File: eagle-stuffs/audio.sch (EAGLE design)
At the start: 35 parts, among them IC1 SSM2211SZ, IC2 TL084P, IC4 DS1804-10k

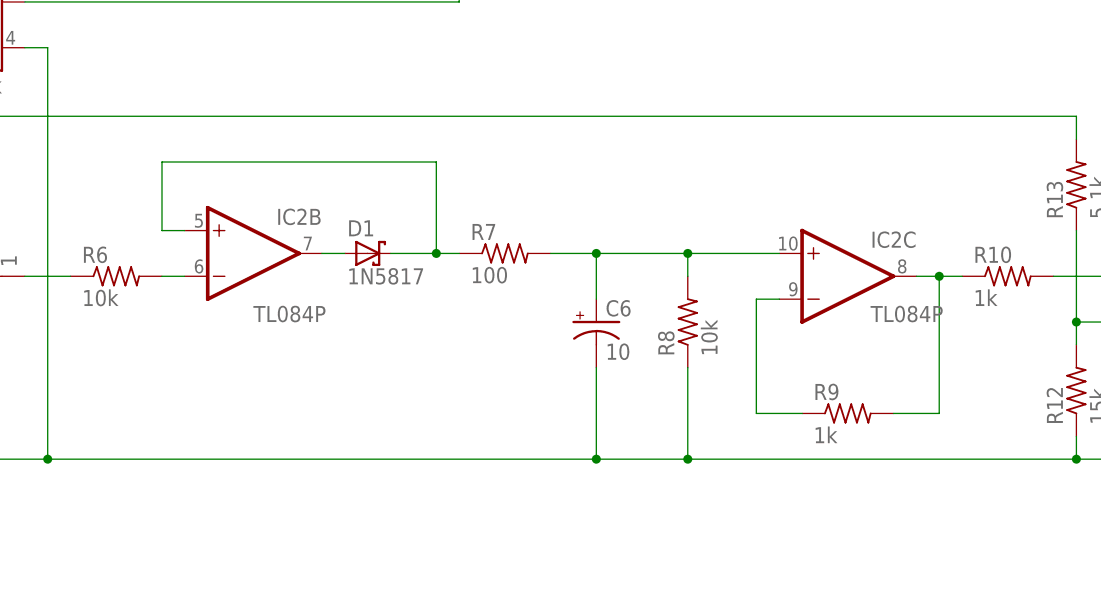
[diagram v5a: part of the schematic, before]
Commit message: Inverted input on follower section for mic
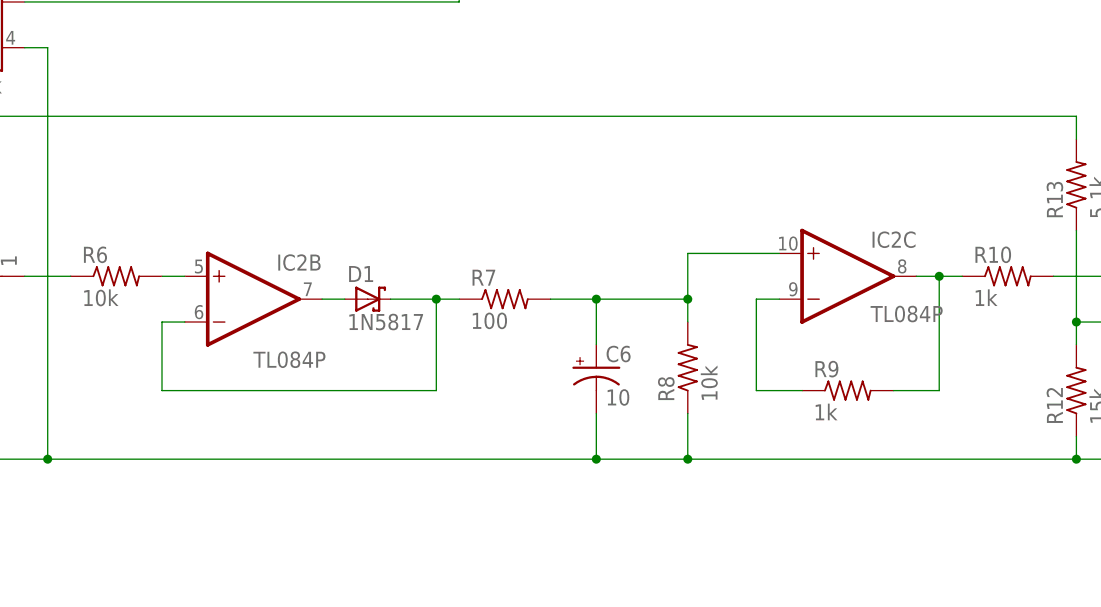
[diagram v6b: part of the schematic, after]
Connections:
- removed net N$13: IC2B.-IN, R6.2
- new net N$18: IC2B.+IN, R6.2
- net N$23: now also IC2B.-IN; no longer IC2B.+IN
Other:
- note added: "D"
- note removed: "C"
- moved on the sheet: C6, D1, IC2B, R7, R8, R9
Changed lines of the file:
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@@
 <text x="193.04" y="25.4" size="2.54" layer="98" font="fixed">Y.A.N.C. (Yet Another Nixie Clock)</text>
 <text x="175.26" y="7.62" size="2.54" layer="98" font="fixed">Licensed under CERN OHL v.1.2 or later</text>
-<text x="264.16" y="7.62" size="2.54" layer="98" font="fixed">C</text>
+<text x="264.16" y="7.62" size="2.54" layer="98" font="fixed">D</text>
 <text x="76.2" y="45.72" size="1.778" layer="98" font="fixed">Preamp</text>
 <text x="132.08" y="45.72" size="1.778" layer="98" font="fixed">Envelope follower</text>
@@
 <instance part="FRAME1" gate="G$2" x="172.72" y="0"/>
 <instance part="IC2" gate="A" x="83.82" y="71.12"/>
-<instance part="IC2" gate="B" x="129.54" y="73.66" smashed="yes">
-<attribute name="NAME" x="132.08" y="76.835" size="1.778" layer="95"/>
-<attribute name="VALUE" x="129.54" y="66.04" size="1.778" layer="96"/>
+<instance part="IC2" gate="B" x="129.54" y="68.58" smashed="yes">
+<attribute name="NAME" x="132.08" y="71.755" size="1.778" layer="95"/>
+<attribute name="VALUE" x="129.54" y="60.96" size="1.778" layer="96"/>
 </instance>
 <instance part="IC4" gate="1" x="91.44" y="104.14" rot="MR0"/>
@@
 <instance part="C4" gate="G$1" x="38.1" y="68.58" rot="R90"/>
 <instance part="C5" gate="G$1" x="99.06" y="71.12" rot="R90"/>
-<instance part="D1" gate="G$1" x="142.24" y="73.66" smashed="yes">
-<attribute name="NAME" x="139.954" y="75.565" size="1.778" layer="95"/>
-<attribute name="VALUE" x="139.954" y="70.231" size="1.778" layer="96"/>
+<instance part="D1" gate="G$1" x="142.24" y="68.58" smashed="yes">
+<attribute name="NAME" x="139.954" y="70.485" size="1.778" layer="95"/>
+<attribute name="VALUE" x="139.954" y="65.151" size="1.778" layer="96"/>
 </instance>
-<instance part="C6" gate="G$1" x="167.64" y="66.04"/>
+<instance part="C6" gate="G$1" x="167.64" y="60.96"/>
 <instance part="R14" gate="G$1" x="48.26" y="162.56"/>
 <instance part="R2" gate="G$1" x="50.8" y="68.58"/>
 <instance part="R5" gate="G$1" x="81.28" y="81.28"/>
 <instance part="R6" gate="G$1" x="114.3" y="71.12"/>
-<instance part="R7" gate="G$1" x="157.48" y="73.66"/>
+<instance part="R7" gate="G$1" x="157.48" y="68.58"/>
 <instance part="R10" gate="G$1" x="213.36" y="71.12"/>
 <instance part="R11" gate="G$1" x="236.22" y="81.28"/>
@@
 <instance part="R3" gate="G$1" x="58.42" y="81.28" rot="R90"/>
 <instance part="R4" gate="G$1" x="58.42" y="58.42" rot="R90"/>
-<instance part="R8" gate="G$1" x="177.8" y="66.04" rot="R90"/>
+<instance part="R8" gate="G$1" x="177.8" y="60.96" rot="R90"/>
 <instance part="R12" gate="G$1" x="220.98" y="58.42" rot="R90"/>
 <instance part="R13" gate="G$1" x="220.98" y="81.28" rot="R90"/>
-<instance part="R9" gate="G$1" x="195.58" y="55.88"/>
+<instance part="R9" gate="G$1" x="195.58" y="58.42"/>
 <instance part="C1" gate="G$1" x="55.88" y="185.42"/>
 <instance part="C2" gate="G$1" x="35.56" y="162.56" rot="R90"/>
@@
 <pinref part="C6" gate="G$1" pin="-"/>
 <wire x1="106.68" y1="50.8" x2="167.64" y2="50.8" width="0.1524" layer="91"/>
-<wire x1="167.64" y1="50.8" x2="167.64" y2="60.96" width="0.1524" layer="91"/>
+<wire x1="167.64" y1="50.8" x2="167.64" y2="55.88" width="0.1524" layer="91"/>
 <junction x="106.68" y="50.8"/>
 <wire x1="167.64" y1="50.8" x2="177.8" y2="50.8" width="0.1524" layer="91"/>
-<wire x1="177.8" y1="50.8" x2="177.8" y2="60.96" width="0.1524" layer="91"/>
+<wire x1="177.8" y1="50.8" x2="177.8" y2="55.88" width="0.1524" layer="91"/>
 <junction x="167.64" y="50.8"/>
 <wire x1="177.8" y1="50.8" x2="220.98" y2="50.8" width="0.1524" layer="91"/>
@@
 </segment>
 </net>
-<net name="N$13" class="0">
-<segment>
-<pinref part="IC2" gate="B" pin="-IN"/>
-<wire x1="119.38" y1="71.12" x2="121.92" y2="71.12" width="0.1524" layer="91"/>
-<pinref part="R6" gate="G$1" pin="2"/>
-</segment>
-</net>
 <net name="N$17" class="0">
 <segment>
 <pinref part="IC2" gate="B" pin="OUT"/>
 <pinref part="D1" gate="G$1" pin="A"/>
-<wire x1="137.16" y1="73.66" x2="139.7" y2="73.66" width="0.1524" layer="91"/>
+<wire x1="137.16" y1="68.58" x2="139.7" y2="68.58" width="0.1524" layer="91"/>
 </segment>
 </net>
 <net name="N$23" class="0">
 <segment>
-<pinref part="IC2" gate="B" pin="+IN"/>
-<wire x1="121.92" y1="76.2" x2="119.38" y2="76.2" width="0.1524" layer="91"/>
-<wire x1="119.38" y1="76.2" x2="119.38" y2="83.82" width="0.1524" layer="91"/>
-<wire x1="119.38" y1="83.82" x2="149.86" y2="83.82" width="0.1524" layer="91"/>
 <pinref part="D1" gate="G$1" pin="C"/>
 <pinref part="R7" gate="G$1" pin="1"/>
-<wire x1="152.4" y1="73.66" x2="149.86" y2="73.66" width="0.1524" layer="91"/>
-<wire x1="149.86" y1="73.66" x2="144.78" y2="73.66" width="0.1524" layer="91"/>
-<wire x1="149.86" y1="83.82" x2="149.86" y2="73.66" width="0.1524" layer="91"/>
-<junction x="149.86" y="73.66"/>
+<wire x1="152.4" y1="68.58" x2="149.86" y2="68.58" width="0.1524" layer="91"/>
+<pinref part="IC2" gate="B" pin="-IN"/>
+<wire x1="149.86" y1="68.58" x2="144.78" y2="68.58" width="0.1524" layer="91"/>
+<wire x1="121.92" y1="66.04" x2="119.38" y2="66.04" width="0.1524" layer="91"/>
+<wire x1="119.38" y1="66.04" x2="119.38" y2="58.42" width="0.1524" layer="91"/>
+<wire x1="119.38" y1="58.42" x2="149.86" y2="58.42" width="0.1524" layer="91"/>
+<wire x1="149.86" y1="58.42" x2="149.86" y2="68.58" width="0.1524" layer="91"/>
+<junction x="149.86" y="68.58"/>
 </segment>
 </net>
@@
 <segment>
 <pinref part="C6" gate="G$1" pin="+"/>
-<wire x1="162.56" y1="73.66" x2="167.64" y2="73.66" width="0.1524" layer="91"/>
-<wire x1="167.64" y1="73.66" x2="167.64" y2="68.58" width="0.1524" layer="91"/>
-<wire x1="167.64" y1="73.66" x2="177.8" y2="73.66" width="0.1524" layer="91"/>
-<wire x1="177.8" y1="73.66" x2="177.8" y2="71.12" width="0.1524" layer="91"/>
-<junction x="167.64" y="73.66"/>
+<wire x1="162.56" y1="68.58" x2="167.64" y2="68.58" width="0.1524" layer="91"/>
+<wire x1="167.64" y1="68.58" x2="167.64" y2="63.5" width="0.1524" layer="91"/>
+<wire x1="167.64" y1="68.58" x2="177.8" y2="68.58" width="0.1524" layer="91"/>
+<wire x1="177.8" y1="68.58" x2="177.8" y2="66.04" width="0.1524" layer="91"/>
+<junction x="167.64" y="68.58"/>
 <pinref part="IC2" gate="C" pin="+IN"/>
+<wire x1="177.8" y1="68.58" x2="177.8" y2="73.66" width="0.1524" layer="91"/>
 <wire x1="177.8" y1="73.66" x2="187.96" y2="73.66" width="0.1524" layer="91"/>
-<junction x="177.8" y="73.66"/>
+<junction x="177.8" y="68.58"/>
 <pinref part="R7" gate="G$1" pin="2"/>
 <pinref part="R8" gate="G$1" pin="2"/>
@@
 <net name="N$25" class="0">
 <segment>
-<wire x1="190.5" y1="55.88" x2="185.42" y2="55.88" width="0.1524" layer="91"/>
-<wire x1="185.42" y1="55.88" x2="185.42" y2="68.58" width="0.1524" layer="91"/>
+<wire x1="190.5" y1="58.42" x2="185.42" y2="58.42" width="0.1524" layer="91"/>
+<wire x1="185.42" y1="58.42" x2="185.42" y2="68.58" width="0.1524" layer="91"/>
 <pinref part="IC2" gate="C" pin="-IN"/>
 <wire x1="185.42" y1="68.58" x2="187.96" y2="68.58" width="0.1524" layer="91"/>
@@
 <wire x1="208.28" y1="71.12" x2="205.74" y2="71.12" width="0.1524" layer="91"/>
 <wire x1="205.74" y1="71.12" x2="203.2" y2="71.12" width="0.1524" layer="91"/>
-<wire x1="200.66" y1="55.88" x2="205.74" y2="55.88" width="0.1524" layer="91"/>
-<wire x1="205.74" y1="55.88" x2="205.74" y2="71.12" width="0.1524" layer="91"/>
+<wire x1="200.66" y1="58.42" x2="205.74" y2="58.42" width="0.1524" layer="91"/>
+<wire x1="205.74" y1="58.42" x2="205.74" y2="71.12" width="0.1524" layer="91"/>
 <junction x="205.74" y="71.12"/>
 <pinref part="R10" gate="G$1" pin="1"/>
@@
 </segment>
 </net>
+<net name="N$18" class="0">
+<segment>
+<pinref part="R6" gate="G$1" pin="2"/>
+<pinref part="IC2" gate="B" pin="+IN"/>
+<wire x1="119.38" y1="71.12" x2="121.92" y2="71.12" width="0.1524" layer="91"/>
+</segment>
+</net>

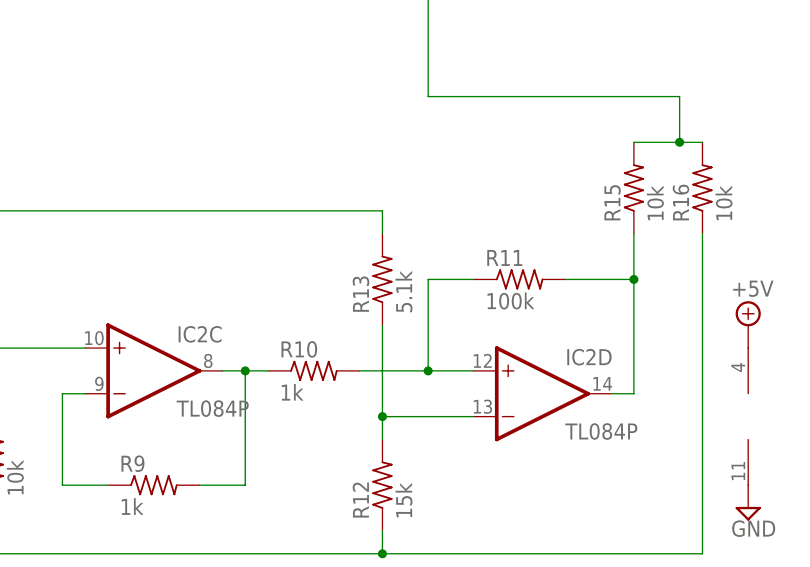
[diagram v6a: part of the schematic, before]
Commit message: Change R13 value
Going at 10k on the digit pot will have the reverse effect on gain and
shutdown the mic.
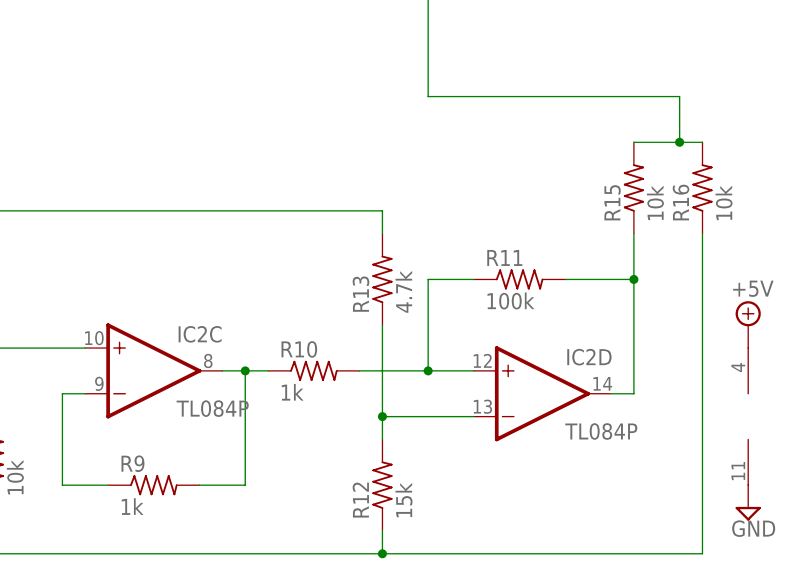
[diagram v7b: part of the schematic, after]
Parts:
- R13: value 5.1k -> 4.7k
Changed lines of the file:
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@@
 <part name="R8" library="rcl" deviceset="R-US_" device="0204/2V" value="10k"/>
 <part name="R12" library="rcl" deviceset="R-US_" device="0204/2V" value="15k"/>
-<part name="R13" library="rcl" deviceset="R-US_" device="0204/2V" value="5.1k"/>
+<part name="R13" library="rcl" deviceset="R-US_" device="0204/2V" value="4.7k"/>
 <part name="R9" library="rcl" deviceset="R-US_" device="0204/2V" value="1k"/>
 <part name="C1" library="rcl" deviceset="CPOL-US" device="E3.5-10" value="220"/>
